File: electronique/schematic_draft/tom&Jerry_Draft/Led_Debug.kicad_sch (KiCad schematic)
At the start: 5 parts, among them IC1301 LP5812CDSDR

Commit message: STM32 KiCAD V5 - 25.09.2024 - Ajout connecteurs TOF, ...
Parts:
- removed IC1301: LP5812CDSDR, SON65P300X300X80-9N-D, symbol LP5812CDSDR:LP5812CDSDR
- added U1301: LP5812ADSDR, LP5812:WSON8_DSD_TEX, symbol LP5812ADSDR:LP5812ADSDR
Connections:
- net +5V: now also U1301.1 (VCC)
- net GND: now also U1301.2 (SYNC), U1301.9 (GND)
- net Led_Debug_SCL: now also U1301.3 (SCL)
- net Led_Debug_SDA: now also U1301.4 (SDA)
- net at D1301.4 (RK), D1302.1 (A), D1303.2 (BK)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: now also U1301.7 (OUT1)
- net at D1301.1 (A), D1302.2 (BK), D1303.3 (GK)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: now also U1301.8 (OUT0)
- net at D1301.2 (BK), D1302.3 (GK), D1303.4 (RK)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: now also U1301.5 (OUT3)
- net at D1301.3 (GK), D1302.4 (RK), D1303.1 (A)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: now also U1301.6 (OUT2)
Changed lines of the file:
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@@
 	(hierarchical_label "Led_Debug_SDA"
 		(shape input)
-		(at 92.71 72.39 180)
+		(at 82.55 69.85 180)
 		(fields_autoplaced yes)
 		(effects
@@
 	(hierarchical_label "Led_Debug_SCL"
 		(shape input)
-		(at 92.71 69.85 180)
+		(at 82.55 67.31 180)
 		(fields_autoplaced yes)
 		(effects
@@
 	(symbol
 		(lib_id "power:+5V")
-		(at 92.71 64.77 90)
+		(at 82.55 62.23 90)
 		(unit 1)
 		(exclude_from_sim no)
@@
 		(fields_autoplaced yes)
 		(property "Reference" "#PWR01301"
-			(at 96.52 64.77 0)
+			(at 86.36 62.23 0)
 			(effects
 				(font
@@
 		)
 		(property "Value" "+5V"
-			(at 88.9 64.7699 90)
+			(at 78.74 62.2299 90)
 			(effects
 				(font
@@
 		)
 		(property "Footprint" ""
-			(at 92.71 64.77 0)
+			(at 82.55 62.23 0)
 			(effects
 				(font
@@
 		)
 		(property "Datasheet" ""
-			(at 92.71 64.77 0)
+			(at 82.55 62.23 0)
 			(effects
 				(font
@@
 		)
 		(property "Description" "Power symbol creates a global label with name \"+5V\""
-			(at 92.71 64.77 0)
+			(at 82.55 62.23 0)
 			(effects
 				(font
@@
 	(symbol
 		(lib_id "power:GND")
-		(at 92.71 67.31 270)
+		(at 82.55 64.77 270)
 		(unit 1)
 		(exclude_from_sim no)
@@
 		(fields_autoplaced yes)
 		(property "Reference" "#PWR01302"
-			(at 86.36 67.31 0)
+			(at 76.2 64.77 0)
 			(effects
 				(font
@@
 		)
 		(property "Value" "GND"
-			(at 88.9 67.3099 90)
+			(at 78.74 64.7699 90)
 			(effects
 				(font
@@
 		)
 		(property "Footprint" ""
-			(at 92.71 67.31 0)
+			(at 82.55 64.77 0)
 			(effects
 				(font
@@
 		)
 		(property "Datasheet" ""
-			(at 92.71 67.31 0)
+			(at 82.55 64.77 0)
 			(effects
 				(font
@@
 		)
 		(property "Description" "Power symbol creates a global label with name \"GND\" , ground"
-			(at 92.71 67.31 0)
+			(at 82.55 64.77 0)
 			(effects
 				(font
@@
 	)
 	(symbol
+		(lib_id "LP5812ADSDR:LP5812ADSDR")
+		(at 82.55 62.23 0)
+		(unit 1)
+		(exclude_from_sim no)
+		(in_bom yes)
+		(on_board yes)
+		(dnp no)
+		(fields_autoplaced yes)
+		(property "Reference" "U1301"
+			(at 102.87 52.07 0)
+			(effects
+				(font
+					(size 1.524 1.524)
+				)
+			)
+		)
+		(property "Value" "LP5812ADSDR"
+			(at 102.87 54.61 0)
+			(effects
+				(font
+					(size 1.524 1.524)
+				)
+			)
+		)
+		(property "Footprint" "LP5812:WSON8_DSD_TEX"
+			(at 82.55 62.23 0)
+			(effects
+				(font
+					(size 1.27 1.27)
+					(italic yes)
+				)
+				(hide yes)
+			)
+		)
+		(property "Datasheet" "LP5812ADSDR"
+			(at 82.55 62.23 0)
+			(effects
+				(font
+					(size 1.27 1.27)
+					(italic yes)
+				)
+				(hide yes)
+			)
+		)
+		(property "Description" ""
+			(at 82.55 62.23 0)
+			(effects
+				(font
+					(size 1.27 1.27)
+				)
+				(hide yes)
+			)
+		)
+		(pin "5"
+		)
+		(pin "6"
+		)
+		(pin "4"
+		)
+		(pin "7"
+		)
+		(pin "8"
+		)
+		(pin "2"
+		)
+		(pin "9"
+		)
+		(pin "3"
+		)
+		(pin "1"
+		)
+		(instances
+			(project ""
+				(path "/d6e3fbeb-d028-494d-83bf-2e4a8b12578d/efa0feee-f3fd-4a3d-b19b-a83f1ab7d3a0"
+					(reference "U1301")
+					(unit 1)
+				)
+			)
+		)
+	)
+	(symbol
 		(lib_id "power:GND")
-		(at 107.95 87.63 0)
+		(at 123.19 62.23 90)
 		(unit 1)
 		(exclude_from_sim no)
@@
 		(fields_autoplaced yes)
 		(property "Reference" "#PWR01303"
-			(at 107.95 93.98 0)
+			(at 129.54 62.23 0)
 			(effects
 				(font
@@
 		)
 		(property "Value" "GND"
-			(at 107.95 92.71 0)
-			(effects
-				(font
-					(size 1.27 1.27)
-				)
+			(at 127 62.2299 90)
+			(effects
+				(font
+					(size 1.27 1.27)
+				)
+				(justify right)
 			)
 		)
 		(property "Footprint" ""
-			(at 107.95 87.63 0)
+			(at 123.19 62.23 0)
 			(effects
 				(font
@@
 		)
 		(property "Datasheet" ""
-			(at 107.95 87.63 0)
+			(at 123.19 62.23 0)
 			(effects
 				(font
@@
 		)
 		(property "Description" "Power symbol creates a global label with name \"GND\" , ground"
-			(at 107.95 87.63 0)
+			(at 123.19 62.23 0)
 			(effects
 				(font
@@
 					(unit 1)
 				)
-			)
-		)
-	)
-	(symbol
-		(lib_id "LP5812CDSDR:LP5812CDSDR")
-		(at 92.71 64.77 0)
-		(unit 1)
-		(exclude_from_sim no)
-		(in_bom yes)
-		(on_board yes)
-		(dnp no)
-		(fields_autoplaced yes)
-		(property "Reference" "IC1301"
-			(at 107.95 57.15 0)
-			(effects
-				(font
-					(size 1.27 1.27)
-				)
-			)
-		)
-		(property "Value" "LP5812CDSDR"
-			(at 107.95 59.69 0)
-			(effects
-				(font
-					(size 1.27 1.27)
-				)
-			)
-		)
-		(property "Footprint" "SON65P300X300X80-9N-D"
-			(at 119.38 159.69 0)
-			(effects
-				(font
-					(size 1.27 1.27)
-				)
-				(justify left top)
-				(hide yes)
-			)
-		)
-		(property "Datasheet" "https://www.ti.com/lit/ds/symlink/lp5812.pdf"
-			(at 119.38 259.69 0)
-			(effects
-				(font
-					(size 1.27 1.27)
-				)
-				(justify left top)
-				(hide yes)
-			)
-		)
-		(property "Description" "LED Lighting Drivers 4 CHANNEL FLEXLED DRIVER"
-			(at 92.71 64.77 0)
-			(effects
-				(font
-					(size 1.27 1.27)
-				)
-				(hide yes)
-			)
-		)
-		(property "Height" "0.8"
-			(at 119.38 459.69 0)
-			(effects
-				(font
-					(size 1.27 1.27)
-				)
-				(justify left top)
-				(hide yes)
-			)
-		)
-		(property "Manufacturer_Name" "Texas Instruments"
-			(at 119.38 559.69 0)
-			(effects
-				(font
-					(size 1.27 1.27)
-				)
-				(justify left top)
-				(hide yes)
-			)
-		)
-		(property "Manufacturer_Part_Number" "LP5812CDSDR"
-			(at 119.38 659.69 0)
-			(effects
-				(font
-					(size 1.27 1.27)
-				)
-				(justify left top)
-				(hide yes)
-			)
-		)
-		(property "Mouser Part Number" "595-LP5812CDSDR"
-			(at 119.38 759.69 0)
-			(effects
-				(font
-					(size 1.27 1.27)
-				)
-				(justify left top)
-				(hide yes)
-			)
-		)
-		(property "Mouser Price/Stock" "https://www.mouser.co.uk/ProductDetail/Texas-Instruments/LP5812CDSDR?qs=Z%252BL2brAPG1KJw2tcOdz4LQ%3D%3D"
-			(at 119.38 859.69 0)
-			(effects
-				(font
-					(size 1.27 1.27)
-				)
-				(justify left top)
-				(hide yes)
-			)
-		)
-		(property "Arrow Part Number" ""
-			(at 119.38 959.69 0)
-			(effects
-				(font
-					(size 1.27 1.27)
-				)
-				(justify left top)
-				(hide yes)
-			)
-		)
-		(property "Arrow Price/Stock" ""
-			(at 119.38 1059.69 0)
-			(effects
-				(font
-					(size 1.27 1.27)
-				)
-				(justify left top)
-				(hide yes)
-			)
-		)
-		(pin "5"
-		)
-		(pin "9"
-		)
-		(pin "1"
-		)
-		(pin "2"
-		)
-		(pin "8"
-		)
-		(pin "3"
-		)
-		(pin "4"
-		)
-		(pin "7"
-		)
-		(pin "6"
-		)
-		(instances
-			(project "tom&Jerry_Draft"
-				(path "/d6e3fbeb-d028-494d-83bf-2e4a8b12578d/efa0feee-f3fd-4a3d-b19b-a83f1ab7d3a0"
-					(reference "IC1301")
-					(unit 1)
-				)

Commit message: STM32 KiCAD v2.0 x CubeIDE - Pin definitif + schematic reviewed
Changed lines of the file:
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@@
+	(wire
+		(pts
+			(xy 62.23 64.77) (xy 82.55 64.77)
+		)
+		(stroke
+			(width 0)
+			(type default)
+		)
+	)
 	(wire
 		(pts
@@
 		(pts
 			(xy 147.32 88.9) (xy 161.29 88.9)
+		)
+		(stroke
+			(width 0)
+			(type default)
+		)
+	)
+	(wire
+		(pts
+			(xy 62.23 62.23) (xy 82.55 62.23)
 		)
 		(stroke
@@
 	(symbol
 		(lib_id "power:+5V")
-		(at 82.55 62.23 90)
+		(at 62.23 62.23 0)
 		(unit 1)
 		(exclude_from_sim no)
@@
 		(fields_autoplaced yes)
 		(property "Reference" "#PWR01301"
-			(at 86.36 62.23 0)
+			(at 62.23 66.04 0)
 			(effects
 				(font
@@
 		)
 		(property "Value" "+5V"
-			(at 78.74 62.2299 90)
-			(effects
-				(font
-					(size 1.27 1.27)
-				)
-				(justify left)
+			(at 62.23 57.15 0)
+			(effects
+				(font
+					(size 1.27 1.27)
+				)
 			)
 		)
 		(property "Footprint" ""
-			(at 82.55 62.23 0)
+			(at 62.23 62.23 0)
 			(effects
 				(font
@@
 		)
 		(property "Datasheet" ""
-			(at 82.55 62.23 0)
+			(at 62.23 62.23 0)
 			(effects
 				(font
@@
 		)
 		(property "Description" "Power symbol creates a global label with name \"+5V\""
-			(at 82.55 62.23 0)
+			(at 62.23 62.23 0)
 			(effects
 				(font
@@
 	(symbol
 		(lib_id "power:GND")
-		(at 82.55 64.77 270)
+		(at 62.23 64.77 0)
 		(unit 1)
 		(exclude_from_sim no)
@@
 		(fields_autoplaced yes)
 		(property "Reference" "#PWR01303"
-			(at 76.2 64.77 0)
+			(at 62.23 71.12 0)
 			(effects
 				(font
@@
 		)
 		(property "Value" "GND"
-			(at 78.74 64.7699 90)
-			(effects
-				(font
-					(size 1.27 1.27)
-				)
-				(justify right)
+			(at 62.23 69.85 0)
+			(effects
+				(font
+					(size 1.27 1.27)
+				)
 			)
 		)
 		(property "Footprint" ""
-			(at 82.55 64.77 0)
+			(at 62.23 64.77 0)
 			(effects
 				(font
@@
 		)
 		(property "Datasheet" ""
-			(at 82.55 64.77 0)
+			(at 62.23 64.77 0)
 			(effects
 				(font
@@
 		)
 		(property "Description" "Power symbol creates a global label with name \"GND\" , ground"
-			(at 82.55 64.77 0)
-			(effects
-				(font
+			(at 62.23 64.77 0)
+			(effects
+				(font

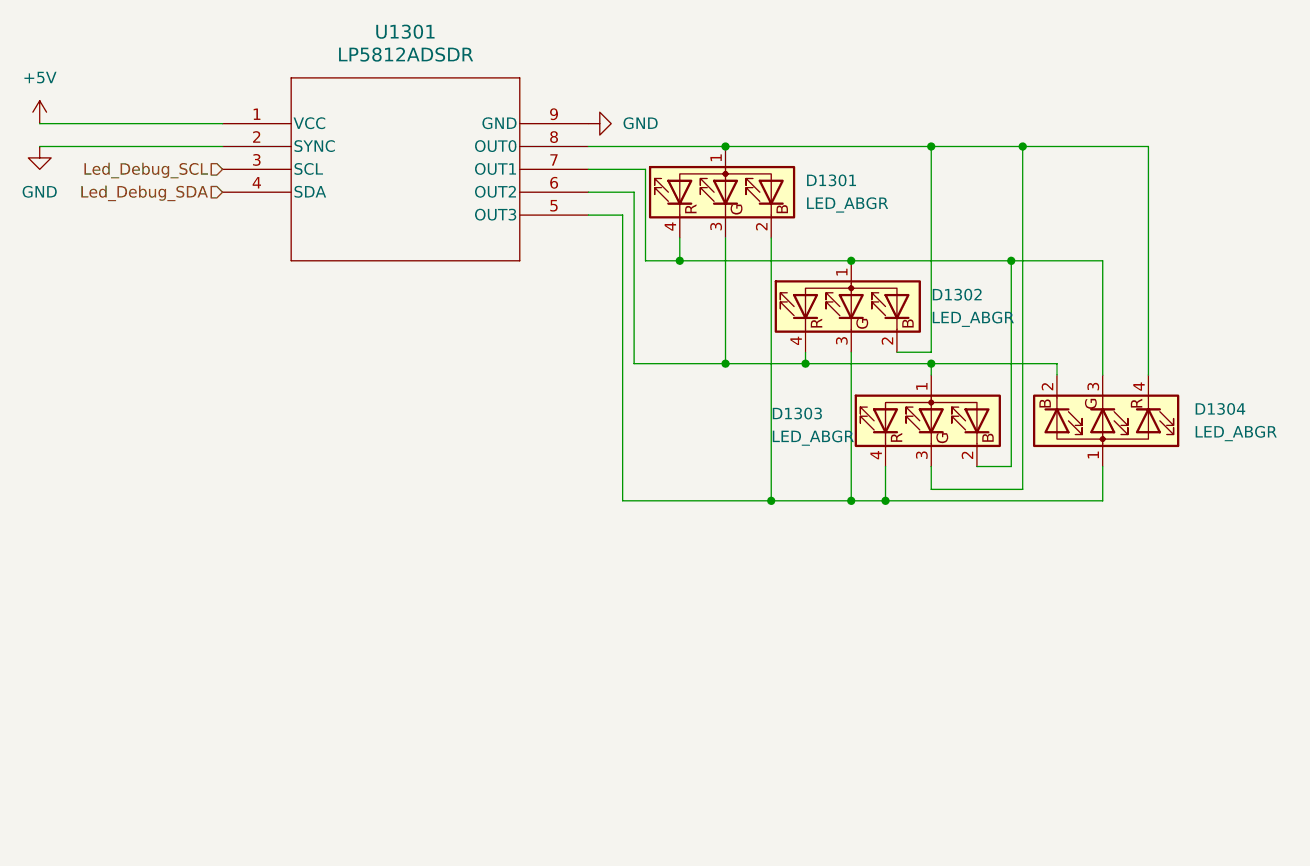
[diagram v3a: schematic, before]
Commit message: Adding footprint V0.1
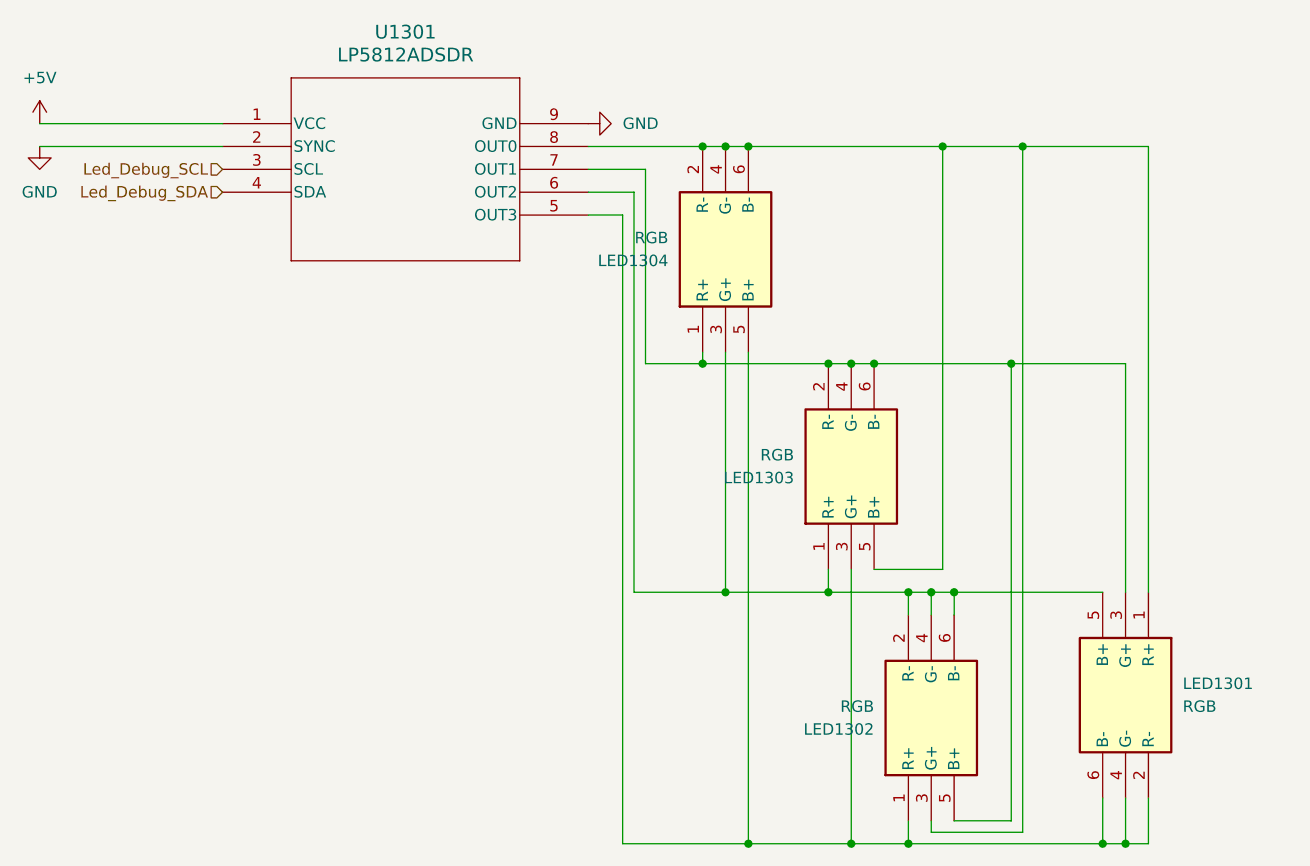
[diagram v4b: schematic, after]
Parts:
- removed D1301, D1302, D1303, D1304: LED_ABGR, symbol Device:LED_ABGR
- added LED1301, LED1302, LED1303, LED1304: RGB, Tom&Jerry:5988G10313F, symbol Tom&Jerry:RGB
- U1301: footprint LP5812:WSON8_DSD_TEX -> Tom&Jerry:WSON8_DSD_TEX
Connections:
- net at U1301.7 (OUT1): now also LED1301.3 (G+), LED1302.5 (B+), LED1303.2 (R-), LED1303.4 (G-), LED1303.6 (B-), LED1304.1 (R+)
- net at U1301.8 (OUT0): now also LED1301.1 (R+), LED1302.3 (G+), LED1303.5 (B+), LED1304.2 (R-), LED1304.4 (G-), LED1304.6 (B-)
- net at U1301.5 (OUT3): now also LED1301.2 (R-), LED1301.4 (G-), LED1301.6 (B-), LED1302.1 (R+), LED1303.3 (G+), LED1304.5 (B+)
- net at U1301.6 (OUT2): now also LED1301.5 (B+), LED1302.2 (R-), LED1302.4 (G-), LED1302.6 (B-), LED1303.1 (R+), LED1304.3 (G+)

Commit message: Ajout V2 TOF + MultiPCB Panalize
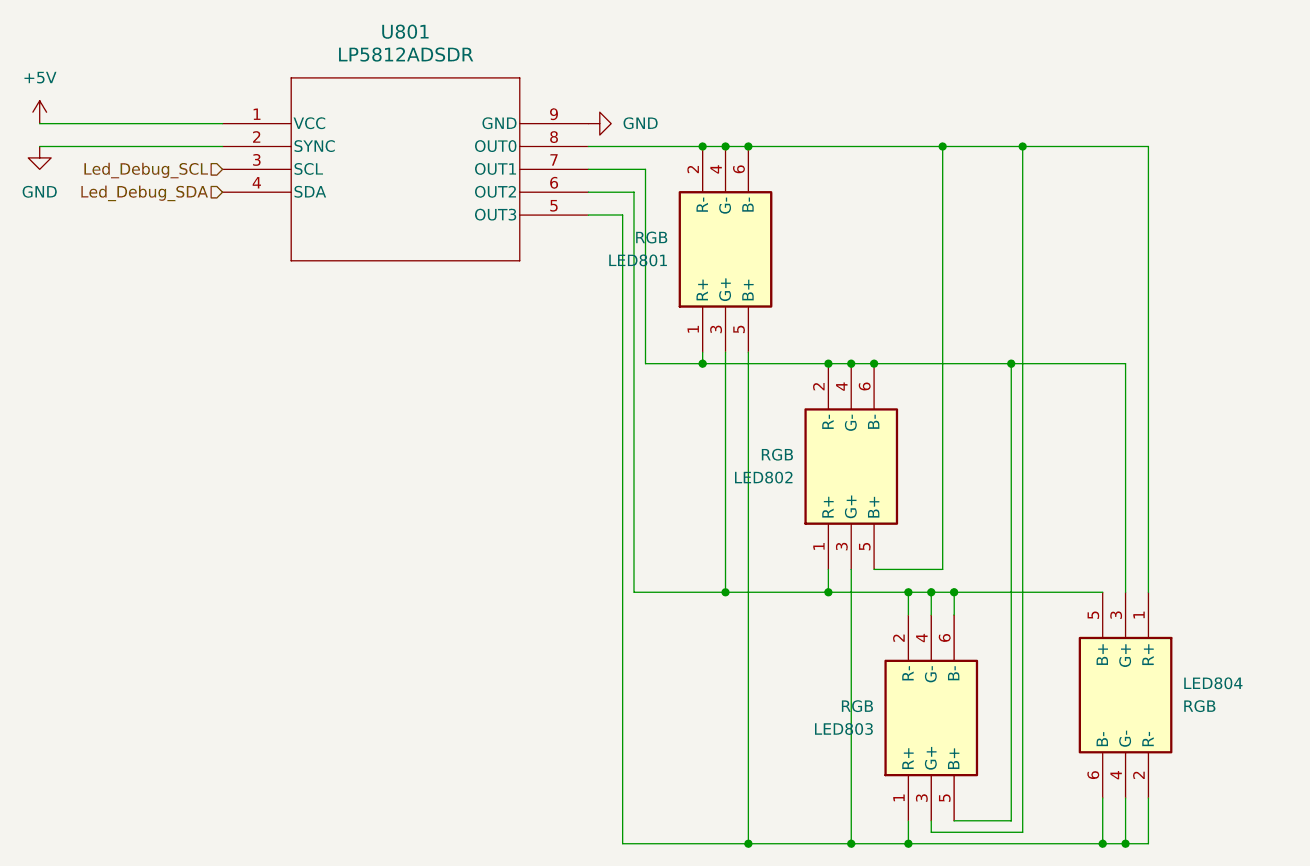
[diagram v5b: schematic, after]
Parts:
- renumbered LED1304 to LED801, LED1303 to LED802, LED1302 to LED803, LED1301 to LED804, U1301 to U801
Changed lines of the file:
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@@
 		(dnp no)
 		(fields_autoplaced yes)
-		(property "Reference" "#PWR01301"
+		(property "Reference" "#PWR0801"
 			(at 62.23 66.04 0)
 			(effects
@@
 			(project "tom&Jerry_Draft"
 				(path "/d6e3fbeb-d028-494d-83bf-2e4a8b12578d/8aa2c92d-cc8b-4d4a-ae4b-287f58b555e7"
-					(reference "#PWR01301")
+					(reference "#PWR0801")
 					(unit 1)
 				)
@@
 		(dnp no)
 		(fields_autoplaced yes)
-		(property "Reference" "LED1301"
+		(property "Reference" "LED804"
 			(at 189.23 124.4599 90)
 			(effects
@@
 			(project ""
 				(path "/d6e3fbeb-d028-494d-83bf-2e4a8b12578d/8aa2c92d-cc8b-4d4a-ae4b-287f58b555e7"
-					(reference "LED1301")
+					(reference "LED804")
 					(unit 1)
 				)
@@
 		(dnp no)
 		(fields_autoplaced yes)
-		(property "Reference" "#PWR01303"
+		(property "Reference" "#PWR0802"
 			(at 62.23 71.12 0)
 			(effects
@@
 			(project "tom&Jerry_Draft"
 				(path "/d6e3fbeb-d028-494d-83bf-2e4a8b12578d/8aa2c92d-cc8b-4d4a-ae4b-287f58b555e7"
-					(reference "#PWR01303")
+					(reference "#PWR0802")
 					(unit 1)
 				)
@@
 		(dnp no)
 		(fields_autoplaced yes)
-		(property "Reference" "U1301"
+		(property "Reference" "U801"
 			(at 102.87 52.07 0)
 			(effects
@@
 			(project "tom&Jerry_Draft"
 				(path "/d6e3fbeb-d028-494d-83bf-2e4a8b12578d/8aa2c92d-cc8b-4d4a-ae4b-287f58b555e7"
-					(reference "U1301")
+					(reference "U801")
 					(unit 1)
 				)
@@
 		(dnp no)
 		(fields_autoplaced yes)
-		(property "Reference" "#PWR01302"
+		(property "Reference" "#PWR0803"
 			(at 129.54 62.23 0)
 			(effects
@@
 			(project "tom&Jerry_Draft"
 				(path "/d6e3fbeb-d028-494d-83bf-2e4a8b12578d/8aa2c92d-cc8b-4d4a-ae4b-287f58b555e7"
-					(reference "#PWR01302")
+					(reference "#PWR0803")
 					(unit 1)
 				)
@@
 		(dnp no)
 		(fields_autoplaced yes)
-		(property "Reference" "LED1303"
+		(property "Reference" "LED802"
 			(at 146.05 101.6001 90)
 			(effects
@@
 			(project "tom&Jerry_Draft"
 				(path "/d6e3fbeb-d028-494d-83bf-2e4a8b12578d/8aa2c92d-cc8b-4d4a-ae4b-287f58b555e7"
-					(reference "LED1303")
+					(reference "LED802")
 					(unit 1)
 				)
@@
 		(dnp no)
 		(fields_autoplaced yes)
-		(property "Reference" "LED1304"
+		(property "Reference" "LED801"
 			(at 132.08 77.4701 90)
 			(effects
@@
 			(project "tom&Jerry_Draft"
 				(path "/d6e3fbeb-d028-494d-83bf-2e4a8b12578d/8aa2c92d-cc8b-4d4a-ae4b-287f58b555e7"
-					(reference "LED1304")
+					(reference "LED801")
 					(unit 1)
 				)
@@
 		(dnp no)
 		(fields_autoplaced yes)
-		(property "Reference" "LED1302"
+		(property "Reference" "LED803"
 			(at 154.94 129.5401 90)
 			(effects
@@
 			(project "tom&Jerry_Draft"
 				(path "/d6e3fbeb-d028-494d-83bf-2e4a8b12578d/8aa2c92d-cc8b-4d4a-ae4b-287f58b555e7"
-					(reference "LED1302")
+					(reference "LED803")
 					(unit 1)
 				)

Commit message: Routage Signal Complet - PCB V2.0
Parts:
- renumbered LED804 to LED803, LED803 to LED804
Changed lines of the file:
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@@
 		(dnp no)
 		(fields_autoplaced yes)
-		(property "Reference" "LED804"
+		(property "Reference" "LED803"
 			(at 189.23 124.4599 90)
 			(effects
@@
 			(project ""
 				(path "/d6e3fbeb-d028-494d-83bf-2e4a8b12578d/8aa2c92d-cc8b-4d4a-ae4b-287f58b555e7"
-					(reference "LED804")
+					(reference "LED803")
 					(unit 1)
 				)
@@
 		(dnp no)
 		(fields_autoplaced yes)
-		(property "Reference" "#PWR0802"
+		(property "Reference" "#PWR0803"
 			(at 62.23 71.12 0)
 			(effects
@@
 			(project "tom&Jerry_Draft"
 				(path "/d6e3fbeb-d028-494d-83bf-2e4a8b12578d/8aa2c92d-cc8b-4d4a-ae4b-287f58b555e7"
-					(reference "#PWR0802")
+					(reference "#PWR0803")
 					(unit 1)
 				)
@@
 		(dnp no)
 		(fields_autoplaced yes)
-		(property "Reference" "#PWR0803"
+		(property "Reference" "#PWR0802"
 			(at 129.54 62.23 0)
 			(effects
@@
 			(project "tom&Jerry_Draft"
 				(path "/d6e3fbeb-d028-494d-83bf-2e4a8b12578d/8aa2c92d-cc8b-4d4a-ae4b-287f58b555e7"
-					(reference "#PWR0803")
+					(reference "#PWR0802")
 					(unit 1)
 				)
@@
 		(dnp no)
 		(fields_autoplaced yes)
-		(property "Reference" "LED803"
+		(property "Reference" "LED804"
 			(at 154.94 129.5401 90)
 			(effects
@@
 			(project "tom&Jerry_Draft"
 				(path "/d6e3fbeb-d028-494d-83bf-2e4a8b12578d/8aa2c92d-cc8b-4d4a-ae4b-287f58b555e7"
-					(reference "LED803")
+					(reference "LED804")
 					(unit 1)
 				)
